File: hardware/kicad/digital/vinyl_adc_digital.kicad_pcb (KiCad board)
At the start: 2 copper layers, 100 x 100 mm, 35 parts, among them J1 CLK SEL, J2 TO PI GPIO, J4 2x8 BUS, U3 74HCT132, U4 74HC4040, U6 74HC157, U8 74HC4049, X1 6.144MHz

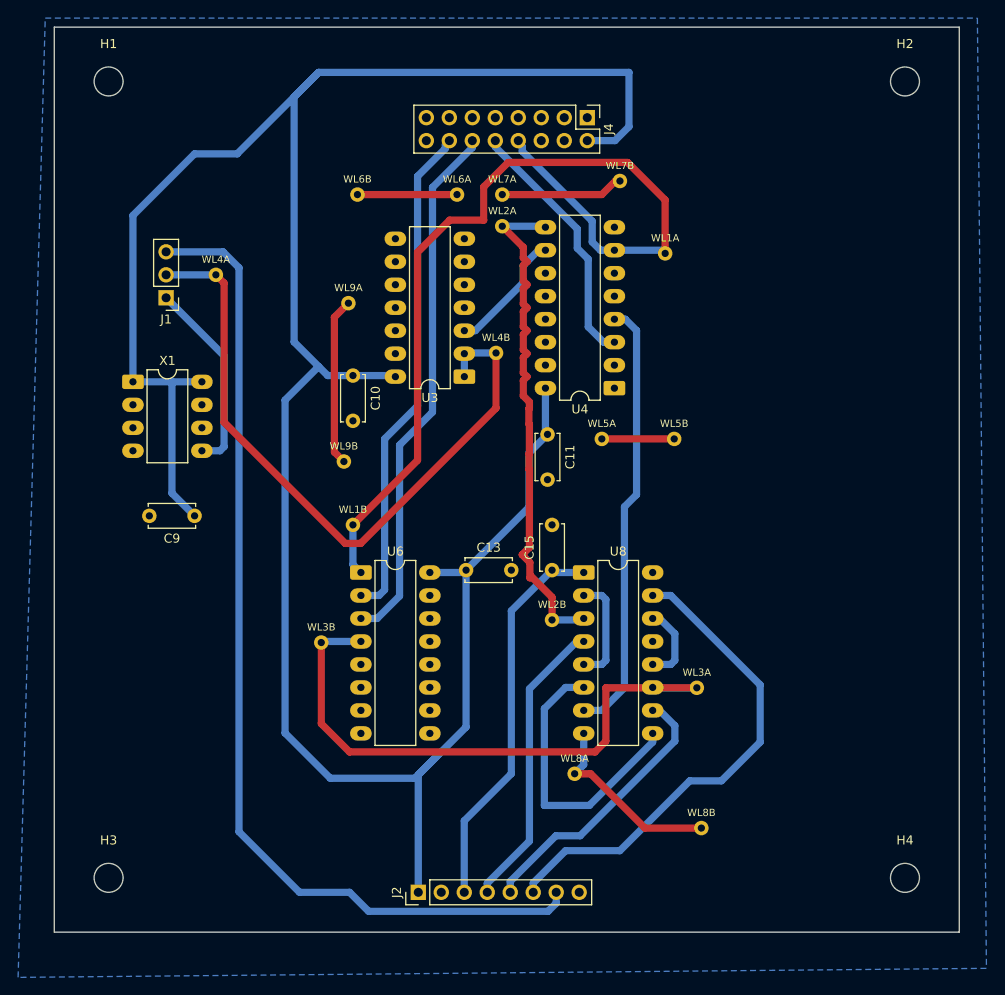
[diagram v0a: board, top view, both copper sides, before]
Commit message: Replace the unobtainable oscillator can with a crystal Pierce
The 6.144 MHz can never turned up, but a bare 2-pin crystal did. The clock
is now a Pierce oscillator -- unbuffered 74HCU04, Rf 1M, Rs 2k2, 27p loads --
drawn by one shared blk_pierce so the digital board rev B, the plug-in
module and the sim_i_pierce bench cannot drift apart.

Rs is 2k2 and not the textbook 1k because the bench showed 1k lets the loop
oscillate at ~30 MHz through the crystal's 5 pF holder capacitance, and a
buffered 74HC04 re-lights that parasitic at any Rs; both findings are in
design-notes section 5 and asserted by the bench (suite 55/55).

The module (hardware/kicad/osc_module/) fills rev A's X1 socket: 40x44 mm
single-sided, routed clean, zero bridges, production files exported. The
digital rev B board carries the 4/4 placement with the bus and holes locked
at the stack coordinates, GND poured, routing still open at 13 links against
a floor of 3 -- same single-sided wall rev A hit, parked for now.

Tooling now runs on Linux too: portable paths in the layout/check/bom
scripts, and check_intent grew Pierce topology assertions.
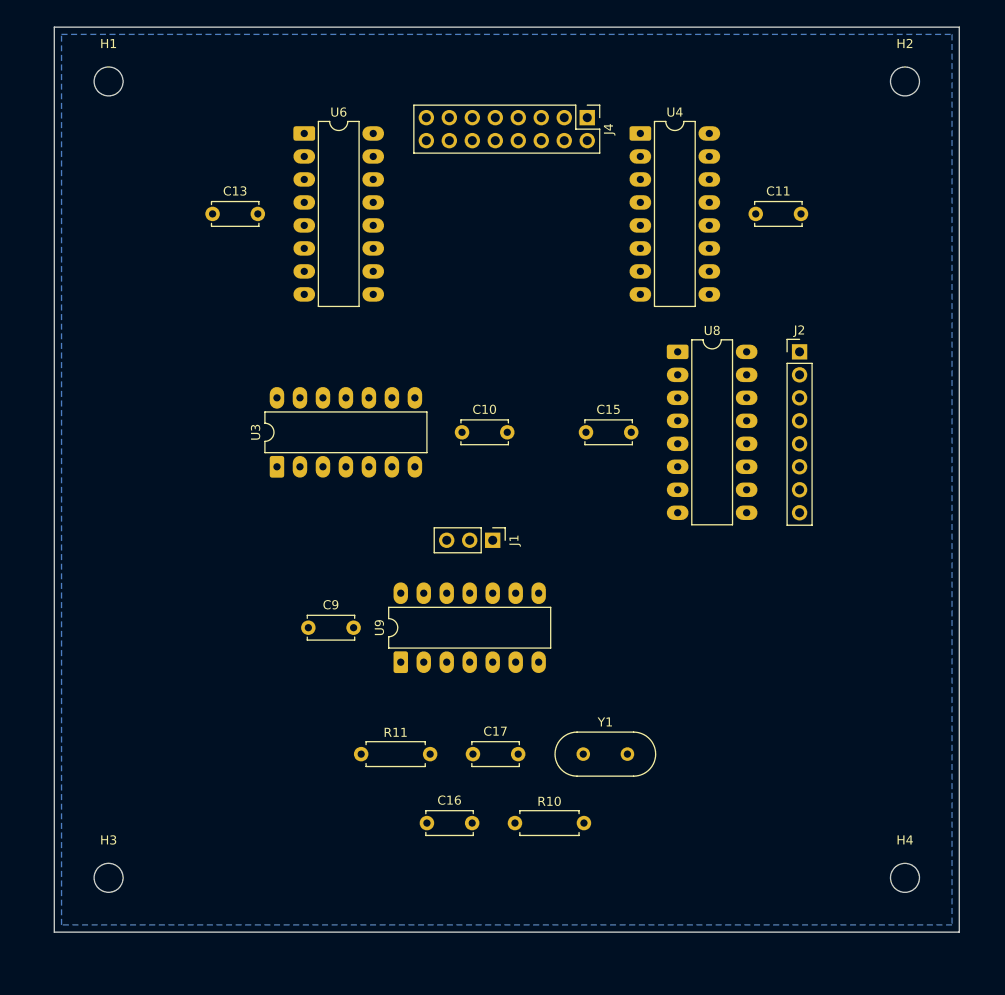
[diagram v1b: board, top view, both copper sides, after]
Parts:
- removed WL1A, WL1B: MCLK, WireLink_TH
- removed WL2A, WL2B: BCLK, WireLink_TH
- removed WL3A, WL3B: DIN, WireLink_TH
- removed WL4A, WL4B: Net-(J1-Pin_2), WireLink_TH
- removed WL5A, WL5B, WL6A, WL6B, WL7A, WL7B, WL8A, WL8B, WL9A, WL9B: GND, WireLink_TH
- removed X1: 6.144MHz, DIP-8_W7.62mm_LongPads
- added C16: 27p, C_Disc_D5.0mm_W2.5mm_P5.00mm, F.Cu at (61.2, 108.0)
- added C17: 27p, C_Disc_D5.0mm_W2.5mm_P5.00mm, F.Cu at (66.3, 100.3)
- added R10: 1M, R_Axial_DIN0207_L6.3mm_D2.5mm_P7.62mm_Horizontal, F.Cu at (70.9, 108.0)
- added R11: 2k2, R_Axial_DIN0207_L6.3mm_D2.5mm_P7.62mm_Horizontal, F.Cu at (53.9, 100.3)
- added U9: 74HCU04, DIP-14_W7.62mm_LongPads, F.Cu at (58.3, 90.2)
- added Y1: 6.144MHz, Crystal_HC49-U_Vertical, F.Cu at (78.5, 100.3)
- moved J2 73.1 mm to (102.4, 55.9), turned to 0 degrees
- moved U6 48.9 mm to (47.6, 31.8)
- moved C13 48.3 mm to (37.5, 40.6)
- moved J1 44.9 mm to (68.4, 76.7), turned to -90 degrees
- moved C11 33.5 mm to (97.5, 40.6), turned to 0 degrees
- moved U4 28.3 mm to (84.8, 31.8), turned to 0 degrees
- moved U8 26.5 mm to (88.9, 55.9)
- moved U3 23.0 mm to (44.6, 68.6), turned to 90 degrees
- moved C9 17.6 mm to (48.1, 86.4), turned to 0 degrees
- moved C15 15.7 mm to (78.8, 64.8), turned to 0 degrees
- moved C10 13.6 mm to (65.1, 64.8), turned to 0 degrees
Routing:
- net +5V: track 286.5 -> 0.00 mm
- net GPCLK0: track 111.4 -> 0.00 mm
- net MCLK: track 103.1 -> 0.00 mm
- net Net-(J1-Pin_2): track 76.1 -> 0.00 mm
- net GND: track 72.5 -> 0.00 mm
- net DIN: track 67.5 -> 0.00 mm
- net QL: track 58.9 -> 0.00 mm
- net BCLK: track 57.5 -> 0.00 mm
- net QR: track 55.5 -> 0.00 mm
- net PI_DIN: track 55.3 -> 0.00 mm
- net LRCLK: track 48.5 -> 0.00 mm
- net +3V3: track 43.2 -> 0.00 mm
- net PI_BCLK: track 32.6 -> 0.00 mm
- net Net-(U8-Pad6): track 31.8 -> 0.00 mm
- net PI_LRCLK: track 30.7 -> 0.00 mm
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
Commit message: finished digital addon board
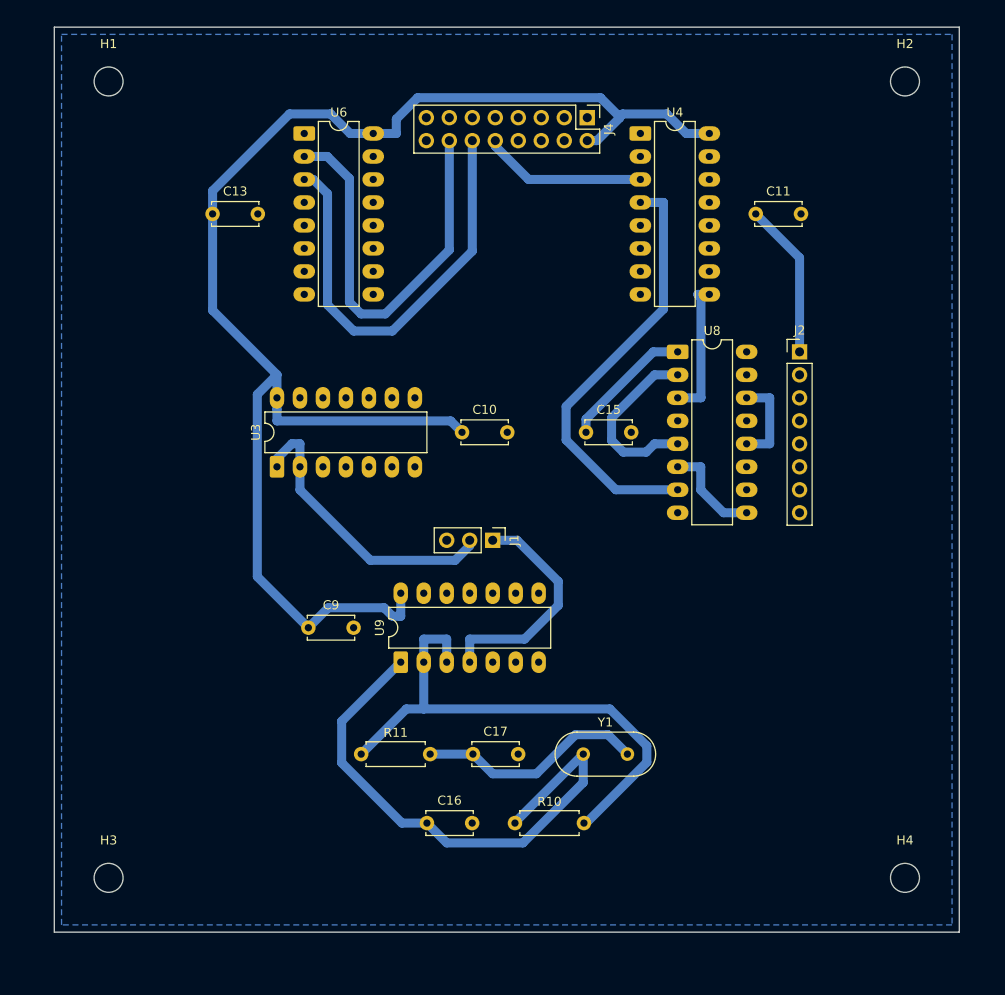
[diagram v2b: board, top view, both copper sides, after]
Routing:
- net +5V: track 0.00 -> 180.4 mm
- net Net-(C16-Pad1): track 0.00 -> 60.8 mm
- net Net-(R10-Pad2): track 0.00 -> 59.7 mm
- net QL: track 0.00 -> 48.6 mm
- net LRCLK: track 0.00 -> 47.9 mm
- net QR: track 0.00 -> 46.3 mm
- net Net-(J1-Pin_2): track 0.00 -> 32.5 mm
- net Net-(J1-Pin_1): track 0.00 -> 25.7 mm
- net Net-(C17-Pad1): track 0.00 -> 25.4 mm
- net Net-(U8-Pad2): track 0.00 -> 20.0 mm
- net PUMP: track 0.00 -> 18.2 mm
- net BCLK: track 0.00 -> 15.4 mm
- net +3V3: track 0.00 -> 14.7 mm
- net Net-(U8-Pad6): track 0.00 -> 11.2 mm
- net Net-(U8-Pad12): track 0.00 -> 10.2 mm

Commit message: Add wire links to digital board and export production files
Board routed with WL pad pairs for the single-sided flow: 48 F.Cu
segments across 6 nets become solder-in wire bridges. DRC clean,
0 unconnected.

Production set for the CNC mill (gerbers + Excellon drill, bits
0.8/1.0/3.2 mm) plus laser DXFs: silk_top for the silkscreen pass and
mask_bottom for UV solder mask ablation. The mask DXF is generated
straight from the pad geometry as closed circles/polylines so xTool
can fill-engrave it (kicad-cli only emits loose LINE segments); MASK
layer = openings, EDGE layer = outline for registration only. Not
mirrored - mirror in xTool with the board copper-side up.
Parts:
- added WL1a: MCLK, WireLink:WireLink_Pad, F.Cu at (79.5, 49.0)
- added WL1b: MCLK, WireLink:WireLink_Pad, F.Cu at (71.5, 36.5)
- added WL2a: CLK6M, WireLink:WireLink_Pad, F.Cu at (97.5, 47.0)
- added WL2b: CLK6M, WireLink:WireLink_Pad, F.Cu at (56.0, 74.0)
- added WL3a: DIN, WireLink:WireLink_Pad, F.Cu at (42.0, 35.5)
- added WL3b: DIN, WireLink:WireLink_Pad, F.Cu at (99.5, 68.5)
- added WL4b: MCLK, WireLink:WireLink_Pad, F.Cu at (43.0, 31.5)
- added WL5a: +3V3, WireLink:WireLink_Pad, F.Cu at (86.5, 53.0)
- added WL5b: +3V3, WireLink:WireLink_Pad, F.Cu at (111.0, 61.0)
- added WL6a: GND, WireLink:WireLink_Pad, F.Cu at (84.0, 61.5)
- added WL6b: GND, WireLink:WireLink_Pad, F.Cu at (84.0, 75.0)
- added WL7a: GND, WireLink:WireLink_Pad, F.Cu at (79.5, 53.0)
- added WL7b: GND, WireLink:WireLink_Pad, F.Cu at (69.5, 53.0)
- added WL8a: PI_DIN, WireLink:WireLink_Pad, F.Cu at (100.0, 58.5)
- added WL8b: PI_DIN, WireLink:WireLink_Pad, F.Cu at (111.0, 68.5)
- added WL9b: GND, WireLink:WireLink_Pad, F.Cu at (60.0, 43.0)
- moved J2 4.00 mm to (106.4, 55.9)
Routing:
- net DIN: track 0.00 -> 129.9 mm
- net CLK6M: track 0.00 -> 104.0 mm
- net MCLK: track 0.00 -> 72.5 mm
- net GPCLK0: track 0.00 -> 53.5 mm
- net GND: track 0.00 -> 44.5 mm, vias 0 -> 2
- net +3V3: track 14.7 -> 55.0 mm
- net +5V: track 180.4 -> 217.6 mm
- net PI_BCLK: track 0.00 -> 34.2 mm
- net PI_DIN: track 0.00 -> 25.9 mm
- net PI_LRCLK: track 0.00 -> 14.2 mm
- net QL: track 48.6 -> 54.8 mm
- net Net-(U8-Pad2): track 20.0 -> 25.1 mm
- net Net-(J1-Pin_1): track 25.7 -> 30.6 mm
- net PUMP: track 18.2 -> 23.1 mm
- net QR: track 46.3 -> 49.5 mm
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
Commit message: Set 0.1 mm solder mask expansion and regenerate production files
Mask openings were exactly pad-sized, leaving no slack for laser-to-board
registration when ablating the UV mask. 0.1 mm global expansion in board
setup; mask_bottom.dxf and gerbers re-exported to match.
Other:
- rule pad_to_mask_clearance: 0 -> 0.1
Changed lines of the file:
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@@
 	)
 	(setup
-		(pad_to_mask_clearance 0)
+		(pad_to_mask_clearance 0.1)
 		(allow_soldermask_bridges_in_footprints no)
 		(tenting
@@
 	)
 	(segment
-		(start 82.56 39.37)
-		(end 74 47.93)
-		(width 1)
-		(layer "B.Cu")
-		(net "LRCLK")
-	)
-	(segment
-		(start 84.76 39.37)
-		(end 82.56 39.37)
-		(width 1)
-		(layer "B.Cu")
-		(net "LRCLK")
-	)
-	(segment
-		(start 78.12 71.12)
-		(end 88.8825 71.12)
-		(width 1)
-		(layer "B.Cu")
-		(net "LRCLK")
-	)
-	(segment
-		(start 74 47.93)
-		(end 74 67)
-		(width 1)
-		(layer "B.Cu")
-		(net "LRCLK")
-	)
-	(segment
-		(start 74 67)
-		(end 78.12 71.12)
-		(width 1)
-		(layer "B.Cu")
-		(net "LRCLK")
-	)
-	(segment
-		(start 92.38 49.53)
-		(end 92 49.91)
-		(width 1)
-		(layer "B.Cu")
-		(net "BCLK")
-	)
-	(segment
-		(start 92 60.0425)
-		(end 91.0825 60.96)
-		(width 1)
-		(layer "B.Cu")
-		(net "BCLK")
-	)
-	(segment
-		(start 92 49.91)
-		(end 92 60.0425)
-		(width 1)
-		(layer "B.Cu")
-		(net "BCLK")
-	)
-	(segment
-		(start 91.0825 60.96)
-		(end 88.8825 60.96)
-		(width 1)
-		(layer "B.Cu")
-		(net "BCLK")
-	)
-	(segment
 		(start 62.43556 58.41)
 		(end 67.905 63.87944)
@@
 	)
 	(segment
+		(start 82.56 39.37)
+		(end 74 47.93)
+		(width 1)
+		(layer "B.Cu")
+		(net "LRCLK")
+	)
+	(segment
+		(start 84.76 39.37)
+		(end 82.56 39.37)
+		(width 1)
+		(layer "B.Cu")
+		(net "LRCLK")
+	)
+	(segment
+		(start 78.12 71.12)
+		(end 88.8825 71.12)
+		(width 1)
+		(layer "B.Cu")
+		(net "LRCLK")
+	)
+	(segment
+		(start 74 47.93)
+		(end 74 67)
+		(width 1)
+		(layer "B.Cu")
+		(net "LRCLK")
+	)
+	(segment
+		(start 74 67)
+		(end 78.12 71.12)
+		(width 1)
+		(layer "B.Cu")
+		(net "LRCLK")
+	)
+	(segment
+		(start 92.38 49.53)
+		(end 92 49.91)
+		(width 1)
+		(layer "B.Cu")
+		(net "BCLK")
+	)
+	(segment
+		(start 92 60.0425)
+		(end 91.0825 60.96)
+		(width 1)
+		(layer "B.Cu")
+		(net "BCLK")
+	)
+	(segment
+		(start 92 49.91)
+		(end 92 60.0425)
+		(width 1)
+		(layer "B.Cu")
+		(net "BCLK")
+	)
+	(segment
+		(start 91.0825 60.96)
+		(end 88.8825 60.96)
+		(width 1)
+		(layer "B.Cu")
+		(net "BCLK")
+	)
+	(segment
